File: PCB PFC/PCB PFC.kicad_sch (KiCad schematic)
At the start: 44 parts, among them J1 INA_1, J2 INA_2, J3 NMJ6HHD2, J4 External_Power, J5 BAT54S_1, J6 BAT54S_2, SW2 SW_Push, U2 L7805, U3 TL082, U4 TL084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

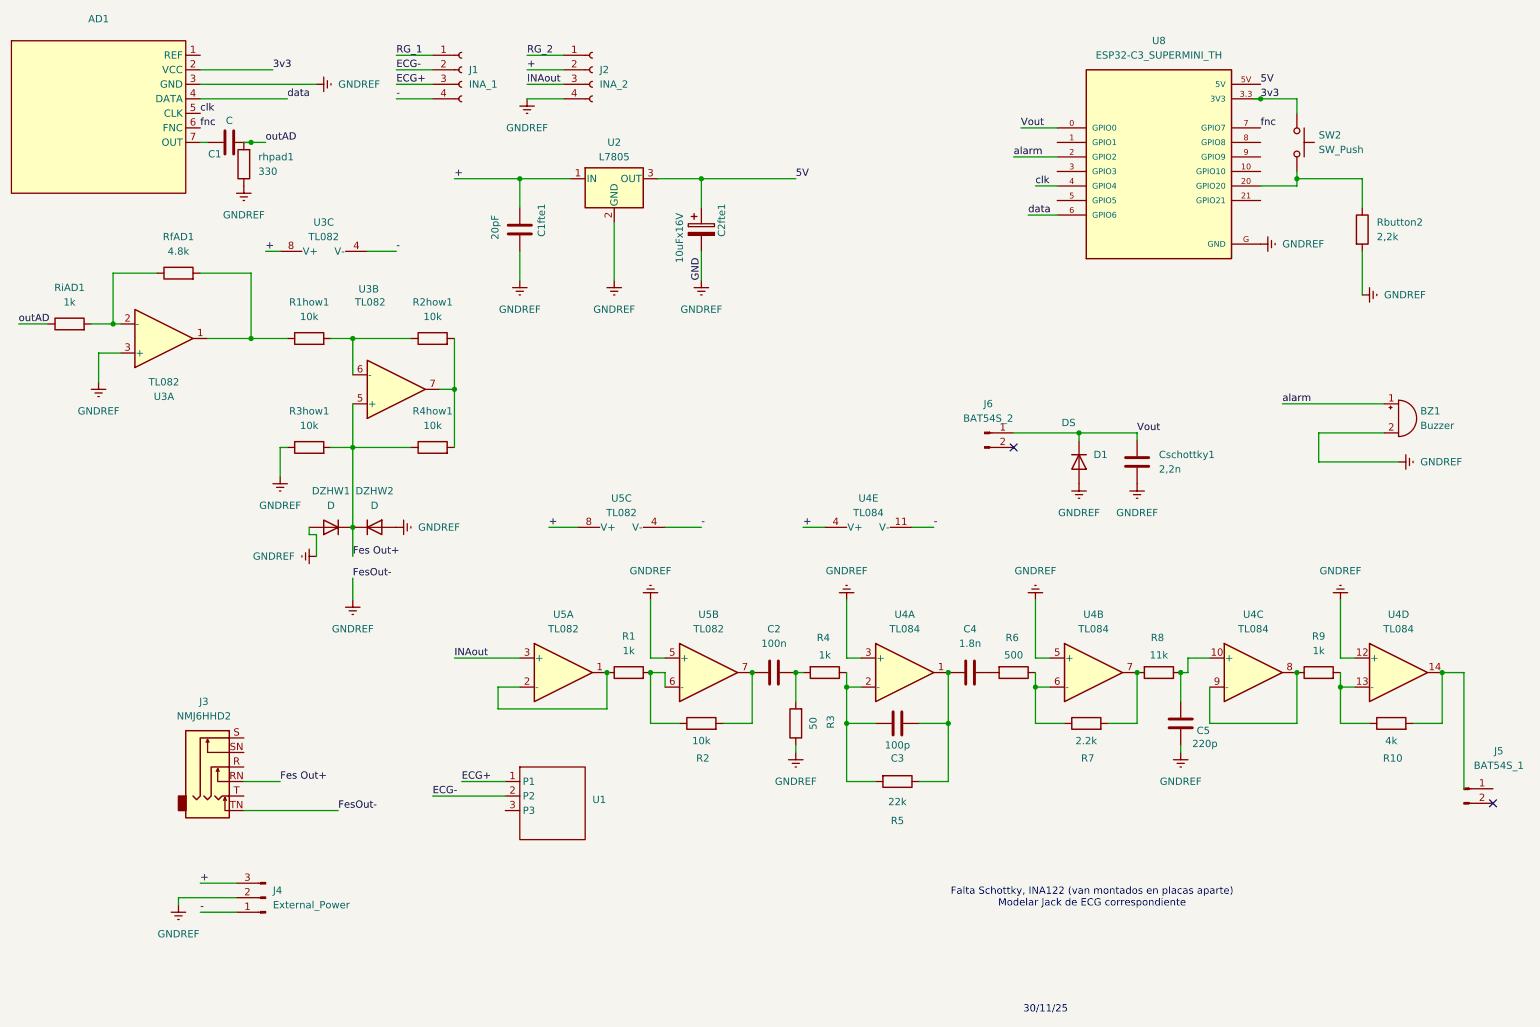
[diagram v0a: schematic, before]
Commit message: Agrego jacks de ECG y librerias
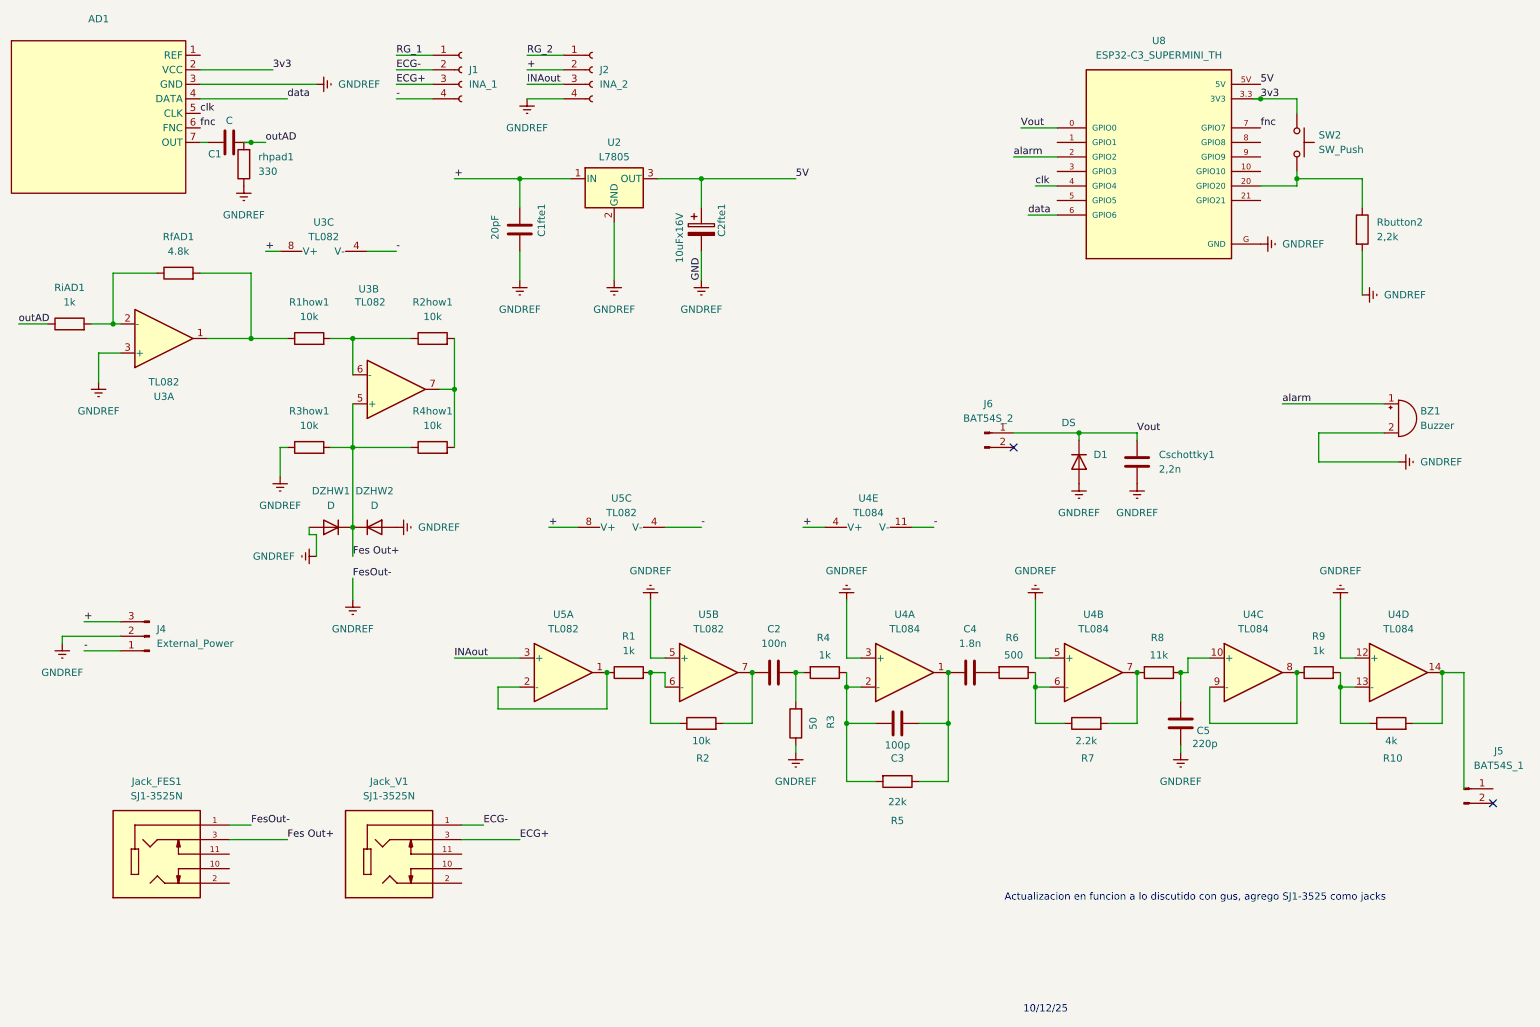
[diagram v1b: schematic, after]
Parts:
- removed J3: NMJ6HHD2, Connector_Audio:Jack_6.35mm_Neutrik_NMJ6HHD2_Horizontal, symbol Connector_Audio:NMJ6HHD2
- removed U1: ~, jackaudio:jack ECG, symbol jackaudio:Jack_ecg
- added Jack_FES1, Jack_V1: SJ1-3525N, SJ1-3525N:CUI_SJ1-3525N, symbol SJ1-3525N:SJ1-3525N
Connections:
- net ECG+: now also Jack_V1.3
- net ECG-: now also Jack_V1.1
- net Fes Out+: now also Jack_FES1.3
- net GNDREF: now also Jack_FES1.1
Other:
- note added: "10/12/25"
- note added: "Actualizacion en funcion a lo discutido con gus, agrego SJ1-3525 como jacks"
- note removed: "30/11/25"
- note removed: "Falta Schottky, INA122 (van montados en placas aparte) Modelar Jack de ECG correspondiente"
- moved on the sheet: J4
